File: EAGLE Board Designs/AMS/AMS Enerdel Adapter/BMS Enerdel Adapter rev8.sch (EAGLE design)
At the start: 48 parts, among them J1 CONNECTOR-1_5222_, J10 CONNECTOR-1_5222_, J11 CONNECTOR-1_5222_, J12 CONNECTOR-1_5222_, J13 CONNECTOR-1_5222_, J14 CONNECTOR-1_5222_, J15 CONNECTOR-1_5222_, J16 CONNECTOR-1_5222_, J17 CONNECTOR-1_5222_, J18 CONNECTOR-1_5222_, J19 CONNECTOR-1_5222_, J2 CONNECTOR-1_5222_, J20 CONNECTOR-1_5222_, J21 CONNECTOR-1_5222_, J22 CONNECTOR-1_5222_, J3 CONNECTOR-1_5222_, J4 CONNECTOR-1_5222_, J5 CONNECTOR-1_5222_, J6 CONNECTOR-1_5222_, J7 CONNECTOR-1_5222_, J8 CONNECTOR-1_5222_, J9 CONNECTOR-1_5222_

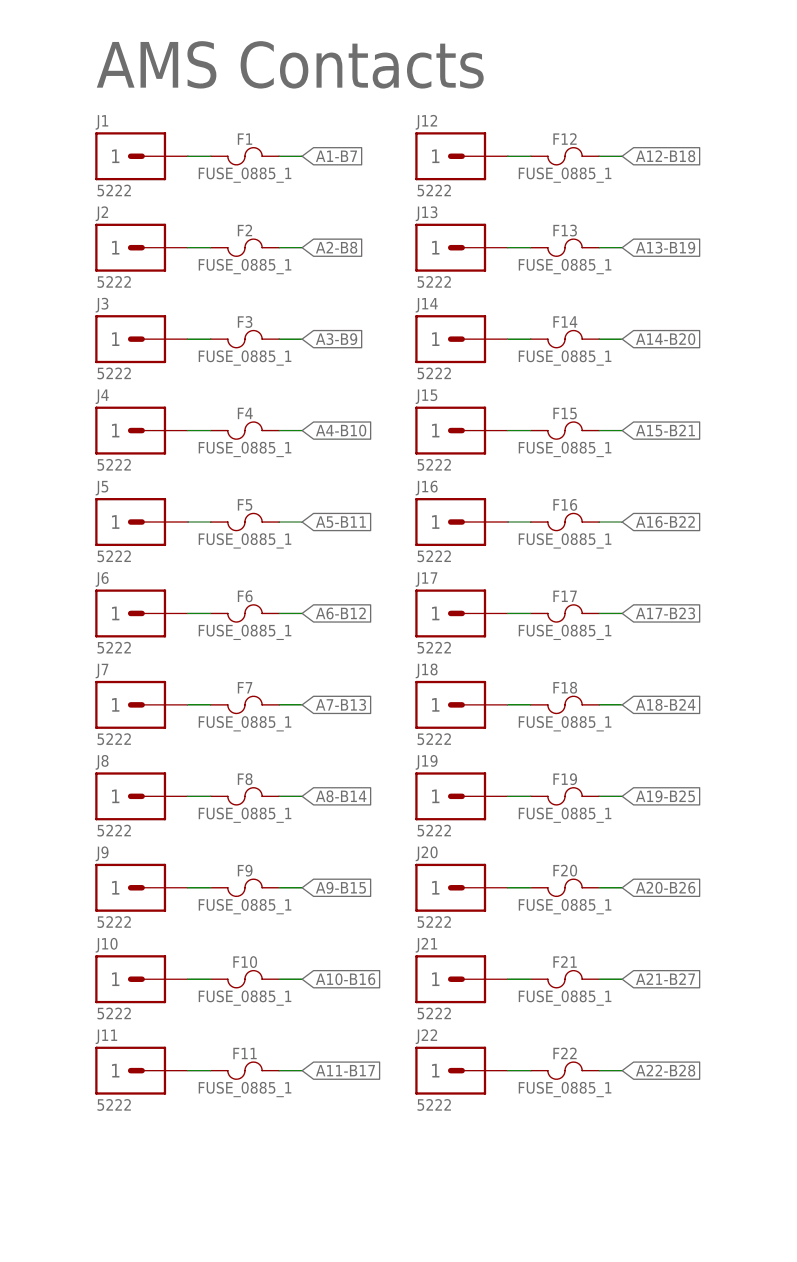
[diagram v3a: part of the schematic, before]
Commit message: changed type of fuses
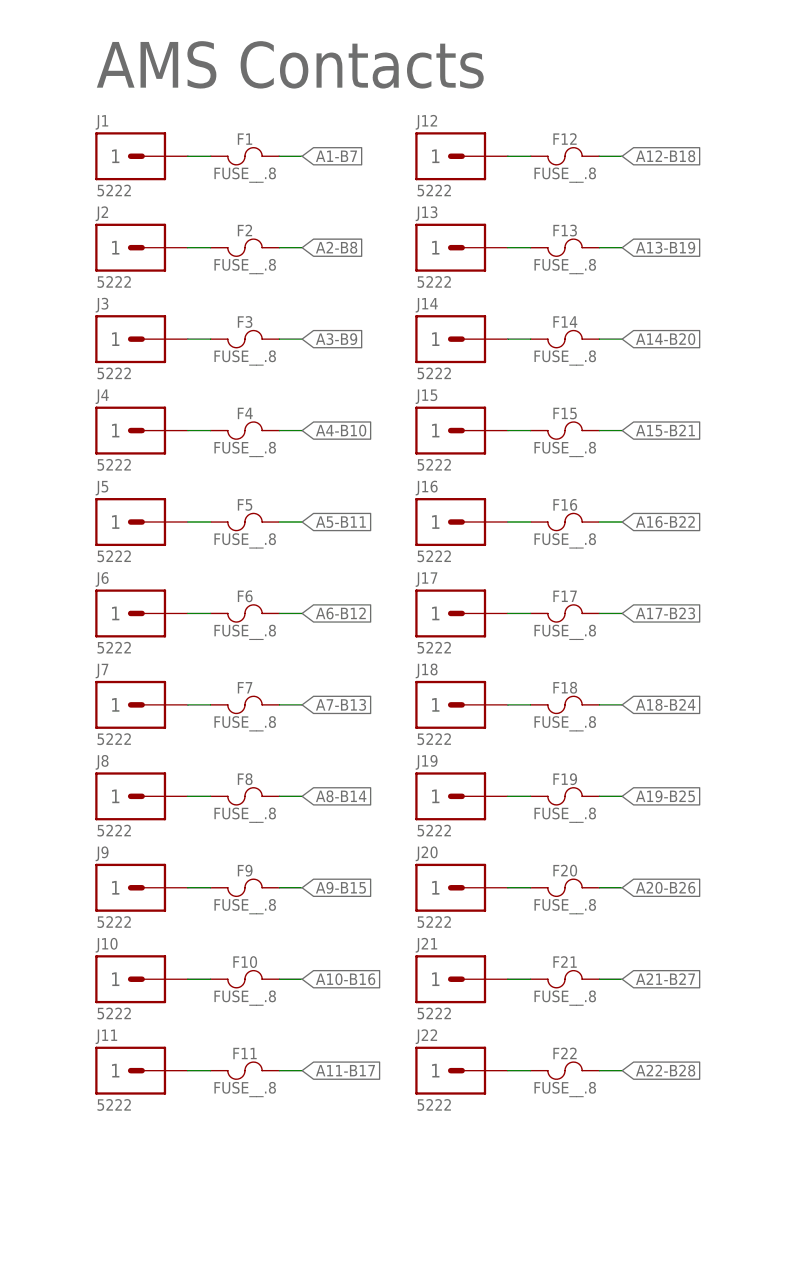
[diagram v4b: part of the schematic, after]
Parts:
- F1, F10, F11, F12, F13, F14, F15, F16, F17, F18, F19, F2, F20, F21, F22, F3, F4, F5, F6, F7, F8, F9: value FUSE_0885_1 -> FUSE__.8; device HyTechDevices:FUSE_0885_1 -> HyTechDevices:FUSE__.8
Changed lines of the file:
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@@
 <drawing>
 <settings>
-<setting alwaysvectorfont="yes"/>
+<setting alwaysvectorfont="no"/>
 <setting verticaltext="up"/>
 </settings>
@@
 <part name="A-CONNECTOR-14-UPPER-IN" library="HyTechDevices" deviceset="CONNECTOR-14_?_*" device="NANOFIT"/>
 <part name="A-CONNECTOR-14-UPPER-OUT" library="HyTechDevices" deviceset="CONNECTOR-14_?_*" device="NANOFIT"/>
-<part name="F1" library="HyTechDevices" deviceset="FUSE_?_*" device="0885" technology="1"/>
-<part name="F2" library="HyTechDevices" deviceset="FUSE_?_*" device="0885" technology="1"/>
-<part name="F3" library="HyTechDevices" deviceset="FUSE_?_*" device="0885" technology="1"/>
-<part name="F4" library="HyTechDevices" deviceset="FUSE_?_*" device="0885" technology="1"/>
-<part name="F5" library="HyTechDevices" deviceset="FUSE_?_*" device="0885" technology="1"/>
-<part name="F6" library="HyTechDevices" deviceset="FUSE_?_*" device="0885" technology="1"/>
-<part name="F7" library="HyTechDevices" deviceset="FUSE_?_*" device="0885" technology="1"/>
-<part name="F8" library="HyTechDevices" deviceset="FUSE_?_*" device="0885" technology="1"/>
-<part name="F9" library="HyTechDevices" deviceset="FUSE_?_*" device="0885" technology="1"/>
-<part name="F10" library="HyTechDevices" deviceset="FUSE_?_*" device="0885" technology="1"/>
-<part name="F11" library="HyTechDevices" deviceset="FUSE_?_*" device="0885" technology="1"/>
-<part name="F12" library="HyTechDevices" deviceset="FUSE_?_*" device="0885" technology="1"/>
-<part name="F13" library="HyTechDevices" deviceset="FUSE_?_*" device="0885" technology="1"/>
-<part name="F14" library="HyTechDevices" deviceset="FUSE_?_*" device="0885" technology="1"/>
-<part name="F15" library="HyTechDevices" deviceset="FUSE_?_*" device="0885" technology="1"/>
-<part name="F16" library="HyTechDevices" deviceset="FUSE_?_*" device="0885" technology="1"/>
-<part name="F17" library="HyTechDevices" deviceset="FUSE_?_*" device="0885" technology="1"/>
-<part name="F18" library="HyTechDevices" deviceset="FUSE_?_*" device="0885" technology="1"/>
-<part name="F19" library="HyTechDevices" deviceset="FUSE_?_*" device="0885" technology="1"/>
-<part name="F20" library="HyTechDevices" deviceset="FUSE_?_*" device="0885" technology="1"/>
-<part name="F21" library="HyTechDevices" deviceset="FUSE_?_*" device="0885" technology="1"/>
-<part name="F22" library="HyTechDevices" deviceset="FUSE_?_*" device="0885" technology="1"/>
+<part name="F1" library="HyTechDevices" deviceset="FUSE_?_*" device="" technology=".8" value="FUSE__.8"/>
+<part name="F2" library="HyTechDevices" deviceset="FUSE_?_*" device="" technology=".8" value="FUSE__.8"/>
+<part name="F3" library="HyTechDevices" deviceset="FUSE_?_*" device="" technology=".8" value="FUSE__.8"/>
+<part name="F4" library="HyTechDevices" deviceset="FUSE_?_*" device="" technology=".8" value="FUSE__.8"/>
+<part name="F5" library="HyTechDevices" deviceset="FUSE_?_*" device="" technology=".8" value="FUSE__.8"/>
+<part name="F6" library="HyTechDevices" deviceset="FUSE_?_*" device="" technology=".8" value="FUSE__.8"/>
+<part name="F7" library="HyTechDevices" deviceset="FUSE_?_*" device="" technology=".8" value="FUSE__.8"/>
+<part name="F8" library="HyTechDevices" deviceset="FUSE_?_*" device="" technology=".8" value="FUSE__.8"/>
+<part name="F9" library="HyTechDevices" deviceset="FUSE_?_*" device="" technology=".8" value="FUSE__.8"/>
+<part name="F10" library="HyTechDevices" deviceset="FUSE_?_*" device="" technology=".8" value="FUSE__.8"/>
+<part name="F11" library="HyTechDevices" deviceset="FUSE_?_*" device="" technology=".8" value="FUSE__.8"/>
+<part name="F12" library="HyTechDevices" deviceset="FUSE_?_*" device="" technology=".8" value="FUSE__.8"/>
+<part name="F13" library="HyTechDevices" deviceset="FUSE_?_*" device="" technology=".8" value="FUSE__.8"/>
+<part name="F14" library="HyTechDevices" deviceset="FUSE_?_*" device="" technology=".8" value="FUSE__.8"/>
+<part name="F15" library="HyTechDevices" deviceset="FUSE_?_*" device="" technology=".8" value="FUSE__.8"/>
+<part name="F16" library="HyTechDevices" deviceset="FUSE_?_*" device="" technology=".8" value="FUSE__.8"/>
+<part name="F17" library="HyTechDevices" deviceset="FUSE_?_*" device="" technology=".8" value="FUSE__.8"/>
+<part name="F18" library="HyTechDevices" deviceset="FUSE_?_*" device="" technology=".8" value="FUSE__.8"/>
+<part name="F19" library="HyTechDevices" deviceset="FUSE_?_*" device="" technology=".8" value="FUSE__.8"/>
+<part name="F20" library="HyTechDevices" deviceset="FUSE_?_*" device="" technology=".8" value="FUSE__.8"/>
+<part name="F21" library="HyTechDevices" deviceset="FUSE_?_*" device="" technology=".8" value="FUSE__.8"/>
+<part name="F22" library="HyTechDevices" deviceset="FUSE_?_*" device="" technology=".8" value="FUSE__.8"/>
 </parts>
 <sheets>

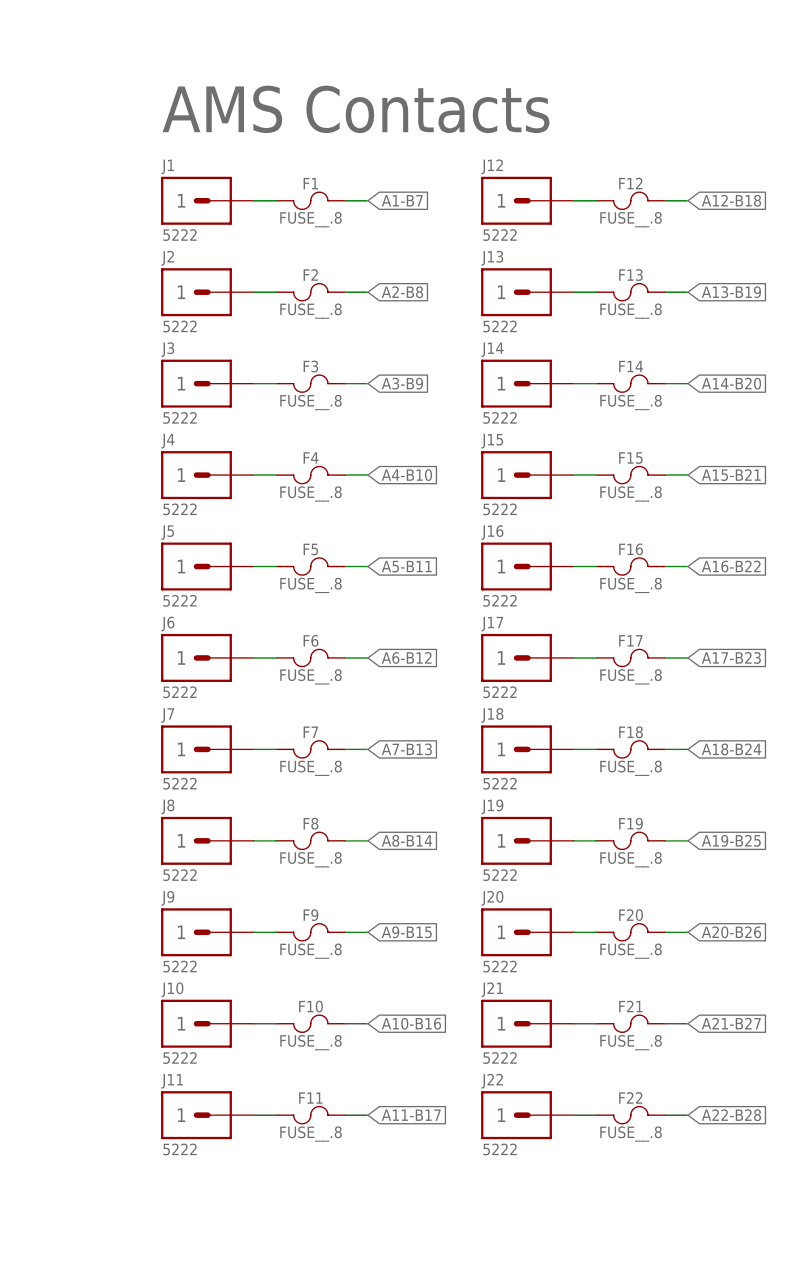
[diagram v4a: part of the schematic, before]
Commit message: updated silkscreen and holes
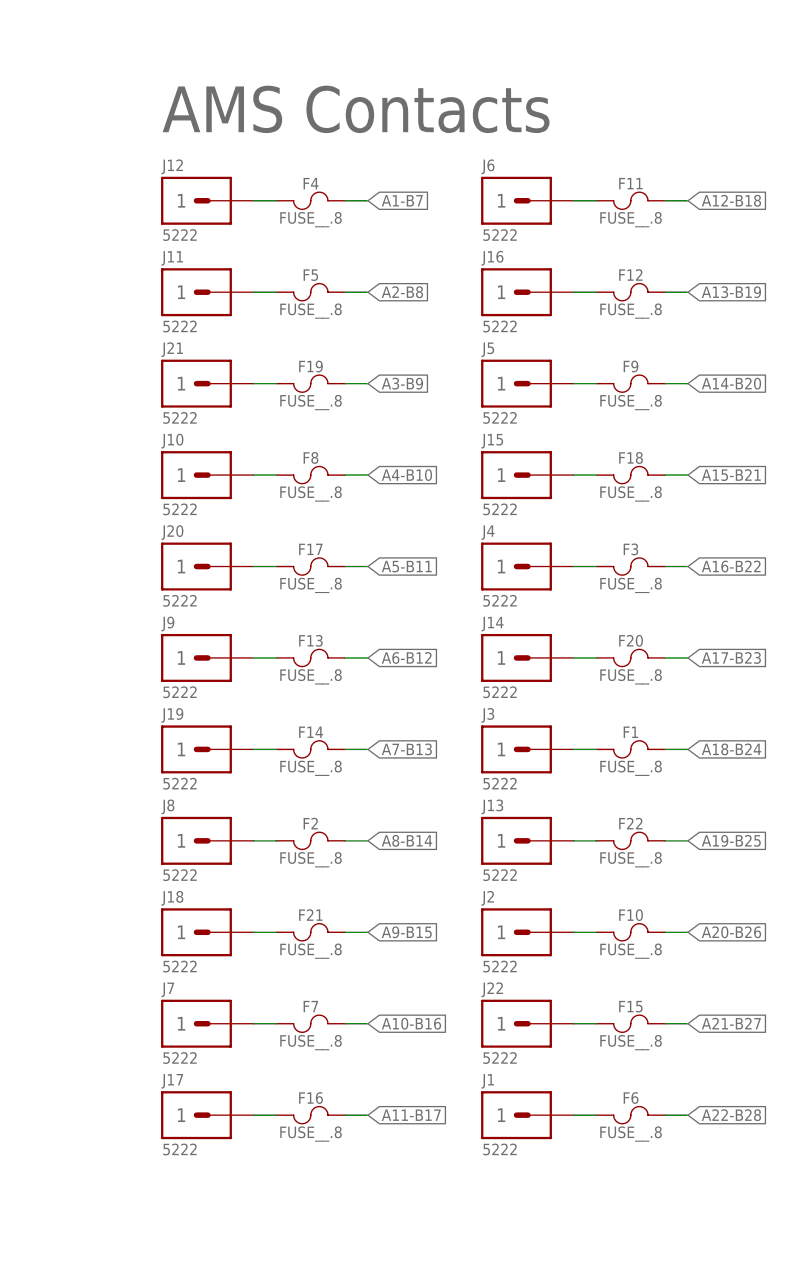
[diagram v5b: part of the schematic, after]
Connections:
- removed net N$13 (its old number): F10.1, J10.1
- new net N$10: F14.1, J19.1
- net A1-B7: now also F4.2; no longer F1.2
- net A10-B16: now also F7.2; no longer F10.2
- net A11-B17: now also F16.2; no longer F11.2
- net A12-B18: now also F11.2; no longer F12.2
- net A13-B19: now also F12.2; no longer F13.2
- net A14-B20: now also F9.2; no longer F14.2
- net A15-B21: now also F18.2; no longer F15.2
- net A16-B22: now also F3.2; no longer F16.2
- net A17-B23: now also F20.2; no longer F17.2
- net A18-B24: now also F1.2; no longer F18.2
- net A19-B25: now also F22.2; no longer F19.2
- net A2-B8: now also F5.2; no longer F2.2
- net A20-B26: now also F10.2; no longer F20.2
- net A21-B27: now also F15.2; no longer F21.2
- net A22-B28: now also F6.2; no longer F22.2
- net A3-B9: now also F19.2; no longer F3.2
- net A4-B10: now also F8.2; no longer F4.2
- net A5-B11: now also F17.2; no longer F5.2
- net A6-B12: now also F13.2; no longer F6.2
- net A7-B13: now also F14.2; no longer F7.2
- net A8-B14: now also F2.2; no longer F8.2
- net A9-B15: now also F21.2; no longer F9.2
- net N$1: now also F4.1, J12.1; no longer F1.1, J1.1
- net N$11: now also F2.1; no longer F8.1
- net N$12: now also F21.1, J18.1; no longer F9.1, J9.1
- net N$14: now also F16.1, J17.1; no longer F11.1, J11.1
- net N$15: now also F6.1, J1.1; no longer F22.1, J22.1
- net N$16: now also F15.1, J22.1; no longer F21.1, J21.1
- net N$17: now also F10.1, J2.1; no longer F20.1, J20.1
- net N$18: now also F22.1, J13.1; no longer F19.1, J19.1
- net N$19: now also F1.1, J3.1; no longer F18.1, J18.1
- net N$2: now also F5.1, J11.1; no longer F2.1, J2.1
- net N$20: now also F20.1, J14.1; no longer F17.1, J17.1
- net N$21: now also F3.1, J4.1; no longer F16.1, J16.1
- net N$22: now also F18.1; no longer F15.1
- net N$23: now also F9.1, J5.1; no longer F14.1, J14.1
- net N$24: now also F11.1, J6.1; no longer F12.1, J12.1
- net N$25: now also F12.1, J16.1; no longer F13.1, J13.1
- net N$3: now also F19.1, J21.1; no longer F3.1, J3.1
- net N$4: now also F8.1, J10.1; no longer F4.1, J4.1
- net N$8: now also F17.1, J20.1; no longer F5.1, J5.1
- net N$9: now also F13.1, J9.1; no longer F6.1, J6.1
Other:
- moved on the sheet: F1, F10, F11, F12, F13, F14, F15, F16, F17, F18, F19, F2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
